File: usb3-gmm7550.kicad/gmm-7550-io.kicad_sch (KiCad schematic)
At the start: 17 parts, among them J4 10144517-061802LF, SW2 SW_Push, SW3 SW_Push

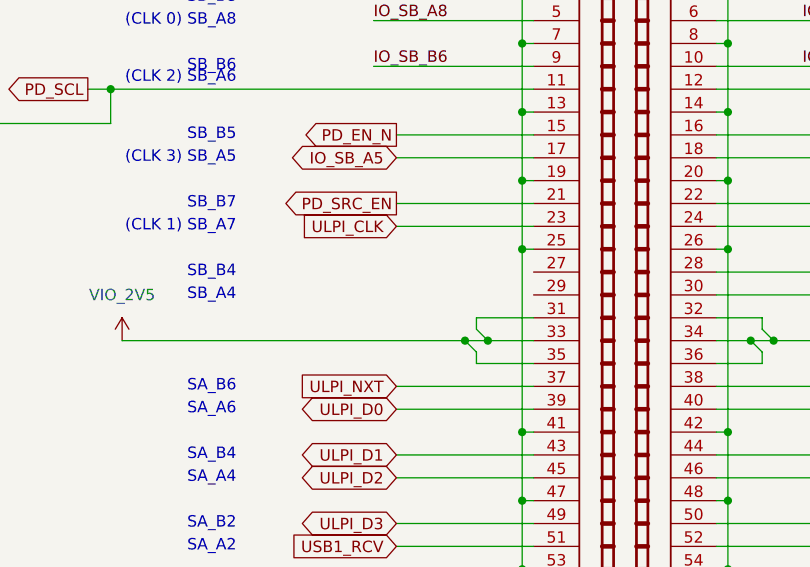
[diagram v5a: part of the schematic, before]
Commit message: Layout [almost] complete -- all connections are routed
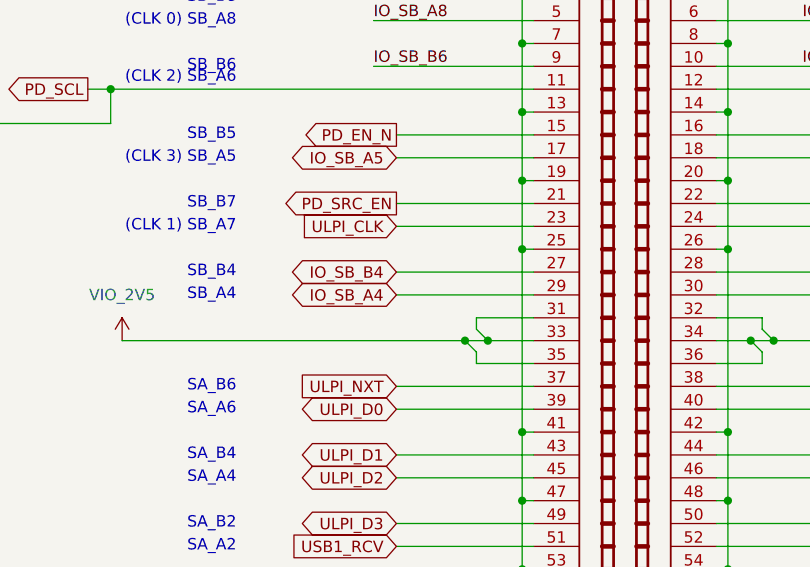
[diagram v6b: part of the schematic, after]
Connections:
- net IO_SB_B4: now reaches J4.27
- net IO_SB_A4: now reaches J4.29
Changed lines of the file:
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@@
 	(wire
 		(pts
+			(xy 119.38 68.58) (xy 134.62 68.58)
+		)
+		(stroke
+			(width 0)
+			(type default)
+		)
+	)
+	(wire
+		(pts
 			(xy 134.62 106.68) (xy 133.35 106.68)
 		)
@@
 	(wire
 		(pts
+			(xy 119.38 66.04) (xy 134.62 66.04)
+		)
+		(stroke
+			(width 0)
+			(type default)
+		)
+	)
+	(wire
+		(pts
 			(xy 133.35 63.5) (xy 133.35 83.82)
 		)
@@
 		)
 	)
+	(global_label "IO_SB_B4"
+		(shape bidirectional)
+		(at 119.38 66.04 180)
+		(fields_autoplaced yes)
+		(effects
+			(font
+				(size 1.27 1.27)
+			)
+			(justify right)
+		)
+		(property "Intersheetrefs" "${INTERSHEET_REFS}"
+			(at 106.454 66.04 0)
+			(effects
+				(font
+					(size 1.27 1.27)
+				)
+				(justify right)
+				(hide yes)
+			)
+		)
+	)
 	(global_label "PD_SDA"
 		(shape bidirectional)
@@
 				(hide yes)
 			)
+		)
+	)
+	(global_label "IO_SB_A4"
+		(shape bidirectional)
+		(at 119.38 68.58 180)
+		(fields_autoplaced yes)
+		(effects
+			(font
+				(size 1.27 1.27)
+			)
+			(justify right)
+		)
+		(property "Intersheetrefs" "${INTERSHEET_REFS}"
+			(at 106.6354 68.58 0)
+			(effects
+				(font
+					(size 1.27 1.27)
+				)
+				(justify right)
+				(hide yes)
+			)
